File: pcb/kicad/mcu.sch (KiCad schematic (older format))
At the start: 1 part, among them U11 LPC1754

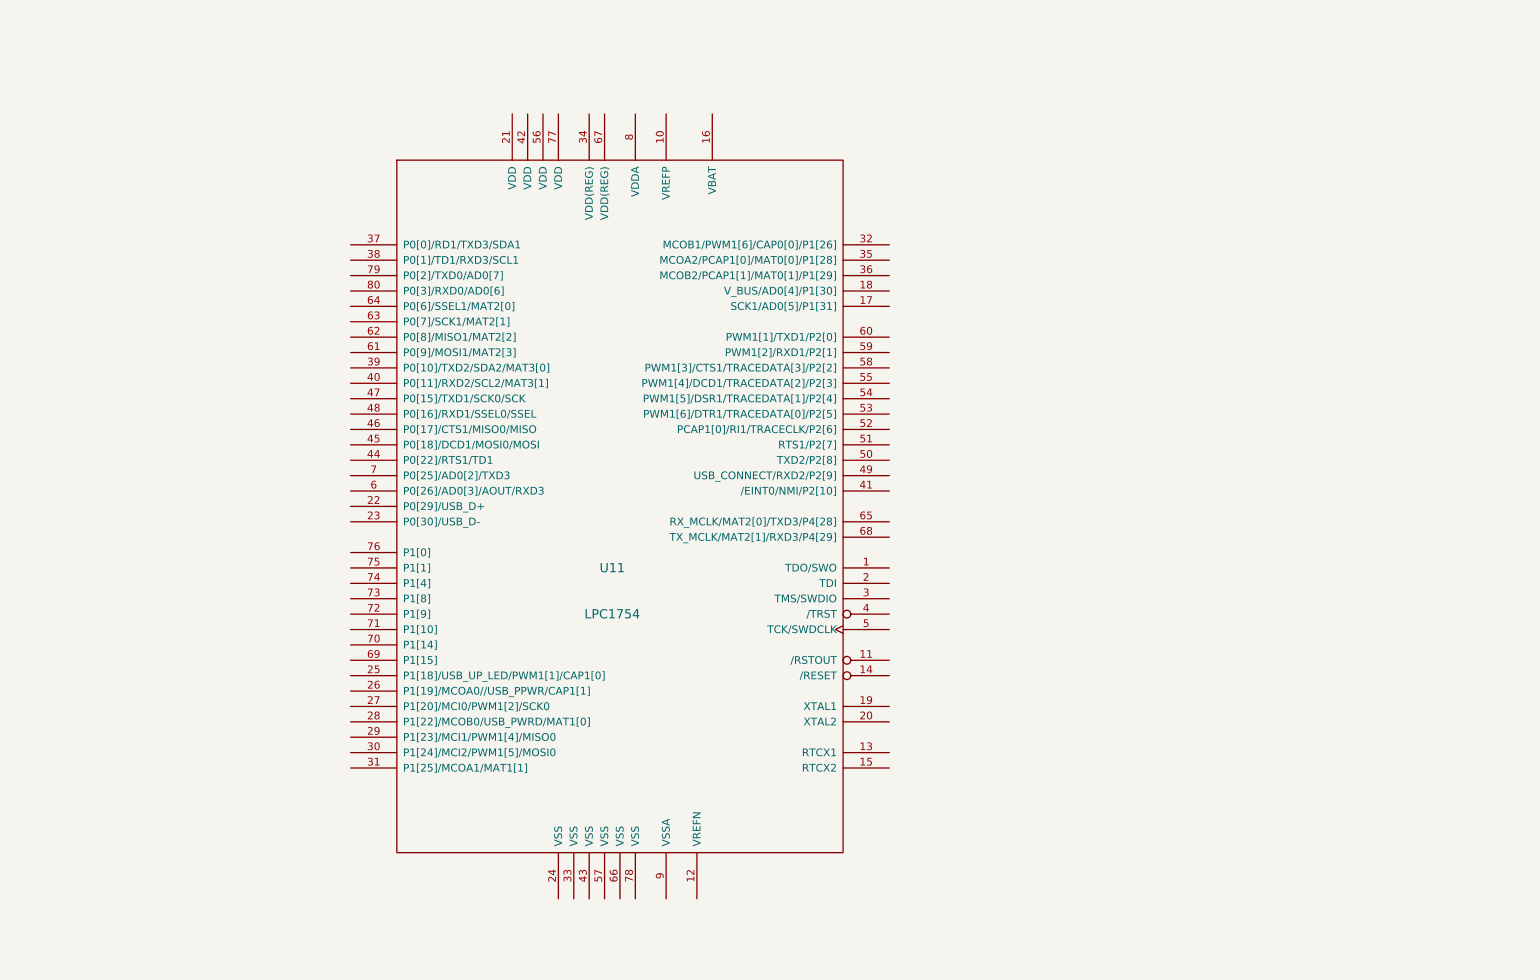
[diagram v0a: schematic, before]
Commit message: clean up AVR code(deprecated), kicad libs, pcb WIP
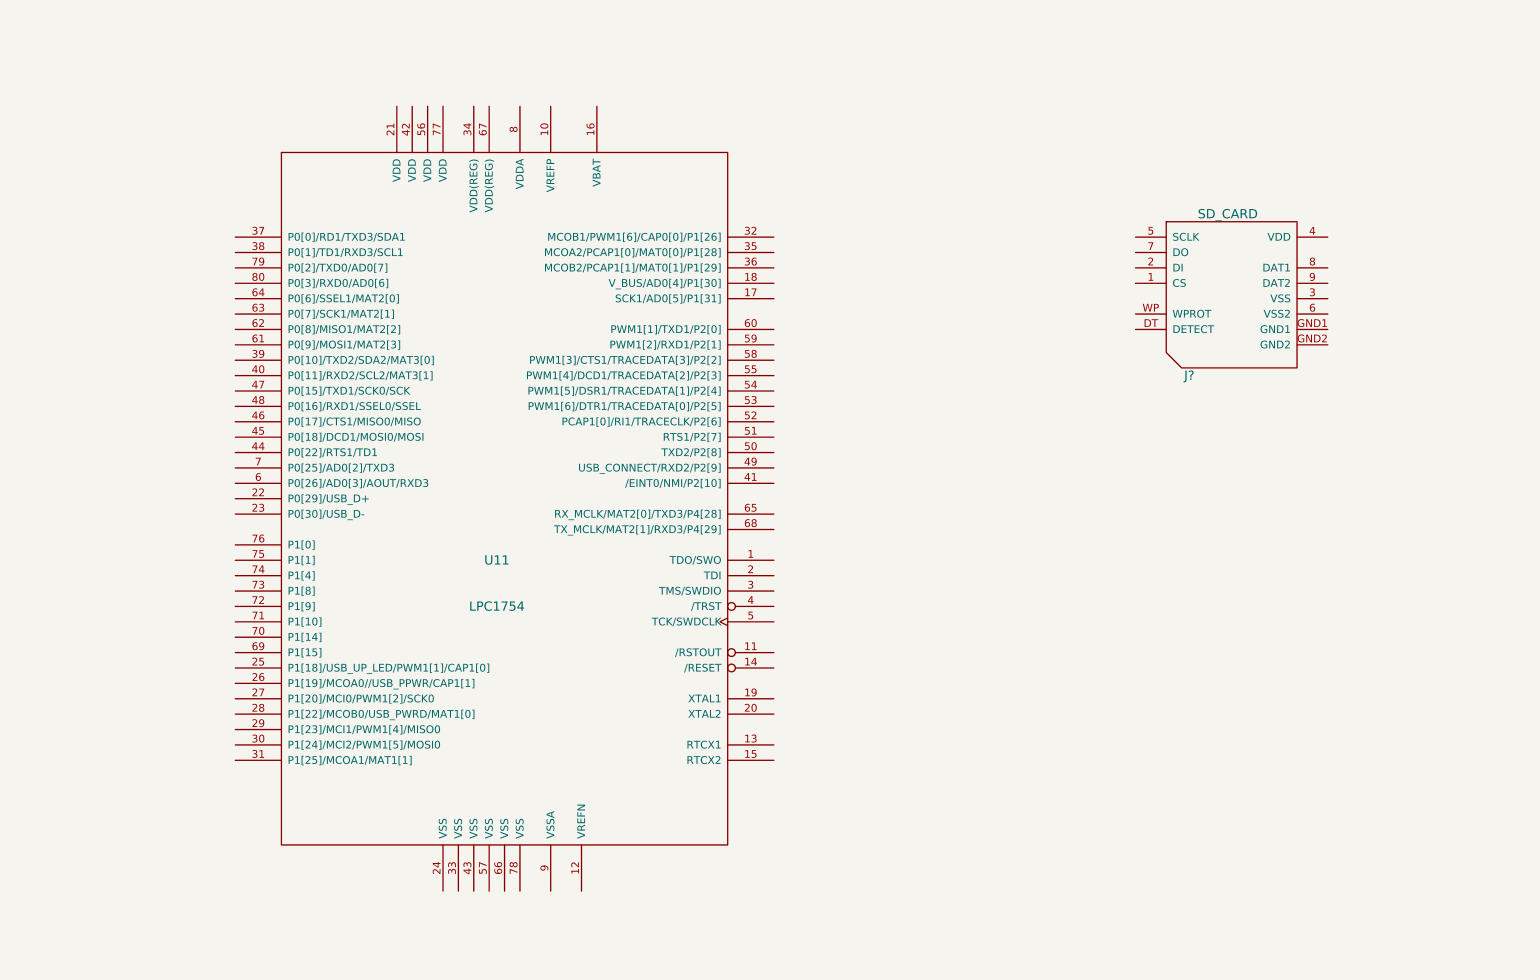
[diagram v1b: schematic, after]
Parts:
- added J?: SD_CARD, symbol SD_CARD
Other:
- moved on the sheet: U11
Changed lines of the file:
@@
-EESchema Schematic File Version 2  date Tue 09 Feb 2010 11:25:34 PM CET
+EESchema Schematic File Version 2  date Wed 24 Mar 2010 11:33:24 PM CET
 LIBS:sd2snes-cache
 LIBS:power
@@
 LIBS:lpc1754
 LIBS:sdcard
-LIBS:testsw
+LIBS:sd_card
+LIBS:cy62148ev30
+LIBS:mt45w8mw16
+LIBS:cs4344
 EELAYER 24  0
 EELAYER END
 $Descr A4 11700 8267
-Sheet 2 5
+Sheet 3 6
 Title ""
 Date "9 feb 2010"
@@
 $EndDescr
 $Comp
+L SD_CARD J?
+U 1 1 4BAA6A9C
+P 8650 2500
+F 0 "J?" H 8400 1950 60  0000 C CNN
+F 1 "SD_CARD" H 8650 3000 60  0000 C CNN
+	1    8650 2500
+	1    0    0    -1
+$EndComp
+$Comp
 L LPC1754 U11
 U 1 1 4B6F321A
-P 4650 3900
-F 0 "U11" H 4650 3500 60  0000 C CNN
-F 1 "LPC1754" H 4650 3200 60  0000 C CNN
-	1    4650 3900
+P 3900 3850
+F 0 "U11" H 3900 3450 60  0000 C CNN
+F 1 "LPC1754" H 3900 3150 60  0000 C CNN
+	1    3900 3850
 	1    0    0    -1
 $EndComp

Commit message: kicad wip
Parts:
- gave numbers to parts that had none: 1
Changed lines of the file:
@@
-EESchema Schematic File Version 2  date Wed 24 Mar 2010 11:33:24 PM CET
-LIBS:sd2snes-cache
+EESchema Schematic File Version 2  date Sat 27 Mar 2010 11:02:39 PM CET
 LIBS:power
 LIBS:device
@@
 LIBS:mt45w8mw16
 LIBS:cs4344
+LIBS:sd2snes-cache
 EELAYER 24  0
 EELAYER END
 $Descr A4 11700 8267
 Sheet 3 6
-Title ""
-Date "9 feb 2010"
-Rev ""
-Comp ""
+Title "sd2snes Mark II"
+Date "27 mar 2010"
+Rev "A"
+Comp "Maximilian Rehkopf"
 Comment1 ""
 Comment2 ""
@@
 $EndDescr
 $Comp
-L SD_CARD J?
+L SD_CARD J2
 U 1 1 4BAA6A9C
 P 8650 2500
-F 0 "J?" H 8400 1950 60  0000 C CNN
+F 0 "J2" H 8400 1950 60  0000 C CNN
 F 1 "SD_CARD" H 8650 3000 60  0000 C CNN
 	1    8650 2500

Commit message: Schematics+PCB WIP
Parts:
- added J3: USB, symbol USB
- added X1, X2: CRYSTAL, symbol CRYSTAL
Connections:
- net +3.3V: now reaches U11.10 (VREFP)
- net +3.3V: now also J2.4 (VDD), U11.21 (VDD), U11.34 (VDD(REG)), U11.42 (VDD), U11.56 (VDD), U11.67 (VDD(REG)), U11.77 (VDD), U11.8 (VDDA)
- net GND: now reaches U11.12 (VREFN)
- net GND: now also J2.3 (VSS), J2.6 (VSS2), J2.GND1, J2.GND2, U11.24 (VSS), U11.33 (VSS), U11.43 (VSS), U11.57 (VSS), U11.66 (VSS), U11.78 (VSS), U11.9 (VSSA)
- net +BATT: now reaches U11.16 (VBAT)
- net MCU_SPI_MOSI: now reaches U11.45 (P0[18]/DCD1/MOSI0/MOSI)
- net MCU_SPI_MISO: now reaches U11.46 (P0[17]/CTS1/MISO0/MISO)
- net MCU_SPI_SCK: now reaches U11.47 (P0[15]/TXD1/SCK0/SCK)
- net MCU_SPI_SS: now reaches U11.48 (P0[16]/RXD1/SSEL0/SSEL)
- net SD_SPI_MOSI: now reaches U11.61 (P0[9]/MOSI1/MAT2[3])
- net SD_SPI_MOSI: now also J2.2 (DI)
- net SD_SPI_MISO: now reaches U11.62 (P0[8]/MISO1/MAT2[2])
- net SD_SPI_MISO: now also J2.7 (DO)
- net SD_SPI_SCK: now reaches U11.63 (P0[7]/SCK1/MAT2[1])
- net SD_SPI_SCK: now also J2.5 (SCLK)
- net SD_SPI_SS: now reaches U11.64 (P0[6]/SSEL1/MAT2[0])
- net SD_SPI_SS: now also J2.1 (CS)
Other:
- moved on the sheet: J2, U11

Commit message: Schematics: connect PSRAM
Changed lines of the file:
@@
-EESchema Schematic File Version 2  date Sun 18 Apr 2010 12:26:45 AM CEST
+EESchema Schematic File Version 2  date Sun 18 Apr 2010 03:00:06 AM CEST
 LIBS:power
 LIBS:device
@@
 Sheet 4 6
 Title "sd2snes Mark II"
-Date "17 apr 2010"
+Date "18 apr 2010"
 Rev "A"
 Comp "Maximilian Rehkopf"
@@
 	7450 2950 7850 2950
 Wire Wire Line
-	7850 2750 7850 2950
+	7850 2950 7850 2750
 Wire Wire Line
 	8850 2650 7750 2650
@@
 	5050 6500 5050 6400
 Wire Wire Line
-	4650 6500 4650 6400
+	4650 6400 4650 6500
 Wire Wire Line
 	4650 6500 5150 6500
@@
 	10200 2550 10200 2300
 Wire Wire Line
-	10200 2950 10100 2950
-Wire Wire Line
-	10200 3550 10200 2950
+	10100 2950 10200 2950
+Wire Wire Line
+	10200 2950 10200 3550
 Connection ~ 10200 3250
 Wire Wire Line
@@
 	6500 2650 7650 2650
 Wire Wire Line
-	7650 2550 7650 2650
-Wire Wire Line
-	8850 2550 7650 2550
+	7650 2650 7650 2550
+Wire Wire Line
+	7650 2550 8850 2550
 Wire Wire Line
 	7450 2850 6500 2850
 Wire Wire Line
-	8850 2750 7850 2750
+	7850 2750 8850 2750
 Wire Wire Line
 	8750 2550 8750 2300
@@
 $EndComp
 $Comp
-L GND #PWR039
+L GND #PWR040
 U 1 1 4BB8BBE8
 P 10200 3550
-F 0 "#PWR039" H 10200 3550 30  0001 C CNN
+F 0 "#PWR040" H 10200 3550 30  0001 C CNN
 F 1 "GND" H 10200 3480 30  0001 C CNN
 	1    10200 3550
@@
 $EndComp
 $Comp
-L +3.3V #PWR040
+L +3.3V #PWR041
 U 1 1 4BB8BBD6
 P 10200 2300
-F 0 "#PWR040" H 10200 2260 30  0001 C CNN
+F 0 "#PWR041" H 10200 2260 30  0001 C CNN
 F 1 "+3.3V" H 10200 2410 30  0000 C CNN
 	1    10200 2300
@@
 $EndComp
 $Comp
-L +3.3V #PWR041
+L +3.3V #PWR042
 U 1 1 4BB8BB64
 P 4450 1200
-F 0 "#PWR041" H 4450 1160 30  0001 C CNN
+F 0 "#PWR042" H 4450 1160 30  0001 C CNN
 F 1 "+3.3V" H 4450 1310 30  0000 C CNN
 	1    4450 1200
@@
 $EndComp
 $Comp
-L GND #PWR042
+L GND #PWR043
 U 1 1 4BB8BB56
 P 4250 6600
-F 0 "#PWR042" H 4250 6600 30  0001 C CNN
+F 0 "#PWR043" H 4250 6600 30  0001 C CNN
 F 1 "GND" H 4250 6530 30  0001 C CNN
 	1    4250 6600
@@
 $EndComp
 $Comp
-L +BATT #PWR043
+L +BATT #PWR044
 U 1 1 4BB8AE61
 P 4150 1200
-F 0 "#PWR043" H 4150 1150 20  0001 C CNN
+F 0 "#PWR044" H 4150 1150 20  0001 C CNN
 F 1 "+BATT" H 4150 1300 30  0000 C CNN
 	1    4150 1200
@@
 $EndComp
 $Comp
-L +3.3V #PWR044
+L +3.3V #PWR045
 U 1 1 4BB8AE12
 P 5050 1200
-F 0 "#PWR044" H 5050 1160 30  0001 C CNN
+F 0 "#PWR045" H 5050 1160 30  0001 C CNN
 F 1 "+3.3V" H 5050 1310 30  0000 C CNN
 	1    5050 1200
@@
 $EndComp
 $Comp
-L GND #PWR045
+L GND #PWR046
 U 1 1 4BAF2DEB
 P 4450 6600
-F 0 "#PWR045" H 4450 6600 30  0001 C CNN
+F 0 "#PWR046" H 4450 6600 30  0001 C CNN
 F 1 "GND" H 4450 6530 30  0001 C CNN
 	1    4450 6600
@@
 $EndComp
 $Comp
-L GND #PWR046
+L GND #PWR047
 U 1 1 4BAF2DE3
 P 4900 6600
-F 0 "#PWR046" H 4900 6600 30  0001 C CNN
+F 0 "#PWR047" H 4900 6600 30  0001 C CNN
 F 1 "GND" H 4900 6530 30  0001 C CNN
 	1    4900 6600

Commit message: pcb wip
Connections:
- net GND: now also J3.4 (GND), J3.5 (Shield_1), J3.6 (Shield_2)
- net at U11.13 (RTCX1): now also X2.2
- net at U11.15 (RTCX2): now also X2.1
- net at U11.18 (V_BUS/AD0[4]/P1[30]): now also J3.1 (Vbus)
- net at U11.19 (XTAL1): now also X1.2
- net at U11.20 (XTAL2): now also X1.1
- net at U11.22 (P0[29]/USB_D+): now also J3.3 (D+)
- net at U11.23 (P0[30]/USB_D-): now also J3.2 (D-)
- net CIC_STATUS: now reaches U11.37 (P0[0]/RD1/TXD3/SDA1)
- net INIT_B+MCU_/IRQ: now reaches U11.41 (/EINT0/NMI/P2[10])
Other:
- moved on the sheet: J2, J3, U11, X1, X2

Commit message: pcb wip
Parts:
- added C34, C35, C36, C37: 22p, symbol C
- X1: value CRYSTAL -> 12MHz
- X2: value CRYSTAL -> 32.768kHz
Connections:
- net CIC_STATUS: now also U11.38 (P0[1]/TD1/RXD3/SCL1); no longer U11.37 (P0[0]/RD1/TXD3/SDA1)
- net GND: now also C34.2, C35.2, C36.2, C37.2
- net at U11.13 (RTCX1): now also X2.1, C36.1; no longer X2.2
- net at U11.15 (RTCX2): now also X2.2, C37.1; no longer X2.1
- net at U11.19 (XTAL1): now also X1.1, C34.1; no longer X1.2
- net at U11.20 (XTAL2): now also X1.2, C35.1; no longer X1.1
- net SNES_/RESET: now reaches U11.36 (MCOB2/PCAP1[1]/MAT0[1]/P1[29])
- net FPGA_CLK: now reaches U11.39 (P0[10]/TXD2/SDA2/MAT3[0])
- net CCLK: now reaches U11.40 (P0[11]/RXD2/SCL2/MAT3[1])
- net DONE: now reaches U11.44 (P0[22]/RTS1/TD1)
- net PROG_B: now reaches U11.65 (RX_MCLK/MAT2[0]/TXD3/P4[28])
- new net CIC_MCLR: U11.37 (P0[0]/RD1/TXD3/SDA1)
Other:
- moved on the sheet: J2, J3
